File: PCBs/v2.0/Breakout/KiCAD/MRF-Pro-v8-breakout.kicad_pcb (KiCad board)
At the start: 2 copper layers, 21 x 15.5 mm, 8 parts, among them J5 FPC 8P Connector, J6 Stemma QT, J7 TFS20L / DTS6012M

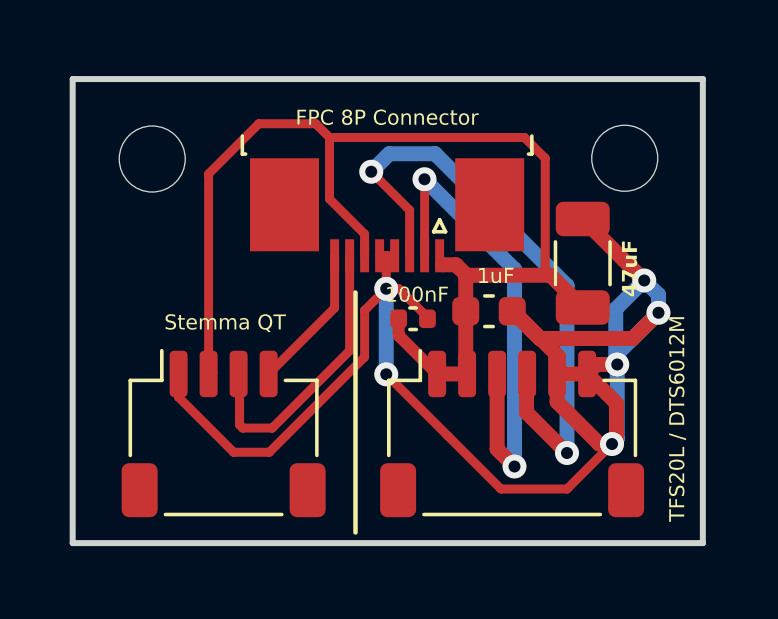
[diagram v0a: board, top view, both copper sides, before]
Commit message: Add the LiDAR LDO EN pulldown and source the breakout BOM
R1 (100k) holds the TLV75533 enable low at power-off. The part has no
internal EN pulldown, so the switched 3.3V rail on FPC pin 1 alone
would not guarantee the regulator shuts down; R1 gives EN a defined
path to ground. Placed and routed next to U1, clear of the laser-pulse
and output-cap clusters. DRC clean.

Add LCSC part numbers (U1, Cin1, Cin2, FB1, R1) for the JLCPCB
assembly BOM.
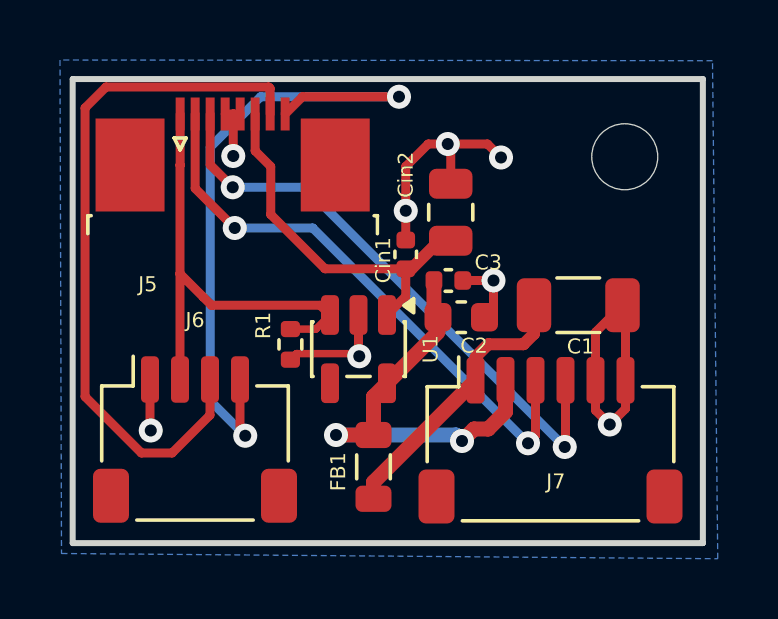
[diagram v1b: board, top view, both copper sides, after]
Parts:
- removed the REF** at (120.0, 125.5)
- removed the REF** at (135.7, 125.5)
- added Cin1: 1uF, Capacitor_SMD:C_0402_1005Metric, F.Cu at (128.4, 128.7)
- added Cin2: 10uF, Capacitor_SMD:C_0805_2012Metric, F.Cu at (129.9, 127.3)
- added FB1: 0, Inductor_SMD:L_0805_2012Metric, F.Cu at (127.3, 135.8)
- added R1: 100k, Resistor_SMD:R_0402_1005Metric, F.Cu at (124.6, 131.7)
- added REF**: MountingHole_2.2mm_M2, MountingHole:MountingHole_2.2mm_M2, F.Cu at (135.7, 125.5)
- added U1: TLV75533, Package_TO_SOT_SMD:SOT-23-5, F.Cu at (126.8, 131.9)
- moved J5 5.53 mm to (122.7, 125.4), turned to 0 degrees
- moved C3 1.73 mm to (129.8, 129.6)
- moved C1 1.41 mm to (134.2, 130.4), turned to 0 degrees
- moved J7 1.30 mm to (133.2, 134.9)
- moved J6 0.97 mm to (121.4, 134.9)
- moved C2 0.95 mm to (130.3, 130.8)
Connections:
- C1 pad 1: /3.3V -> /3V3_LASER
- C2 pad 1: /3.3V -> /3V3_LIDAR
- C3 pad 1: /3.3V -> /3V3_LIDAR
- J5 pad 6: /3.3V -> /VBAT
- J7 pad 1: /3.3V -> /3V3_LASER
- J7 pad 2: /3.3V -> /3V3_LIDAR
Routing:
- net /GND: track 57.1 -> 26.2 mm, vias 6 -> 8
- net /3.3V: track 39.8 -> 15.9 mm
- net Net-(J5-Pin_8): track 4.85 -> 23.1 mm, vias 0 -> 2
- net /3V3_LIDAR: track 0.00 -> 14.5 mm, vias 0 -> 2
- net Net-(J5-Pin_7): track 9.66 -> 23.6 mm
- net /VBAT: track 0.00 -> 12.5 mm
- net /3V3_LASER: track 0.00 -> 9.85 mm
- net Net-(J5-Pin_2): track 16.7 -> 19.3 mm
- net Net-(J5-Pin_3): track 21.2 -> 19.7 mm
- added copper zone on B.Cu, net /GND
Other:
- board text added: "3.3V LASER 3.3v LIDAR RX TX GND GND"
- board text added: "MRF2 Breakout v3"
- board text removed: "3.3V 3.3v RX TX GND GND"
- board text removed: "MRF2 Breakout v2.5"
